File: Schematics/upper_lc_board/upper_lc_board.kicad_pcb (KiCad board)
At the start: 4 copper layers, 69.5 x 60 mm, 125 parts, among them J1 Stack Male Edge Connector, J3 PT1, J4 PT2, J5 SOL_CONN, J6 SOL2_CONN, J7 TC, Q1 MOSFET_BSS138, U1 ESP32-S3-WROOM-1-N16R2, U10 OA-TLV9001IDCK, U11 OA-TLV9001IDCK, U2 CAN_TRX_SN65HVD230DR, U3 PD_D3V3XA4B10LP, U4 PMUX_TPS2121RUXR, U5 TMP117MAIDRVR, U6 TLV75801PDRV, U7 ADC_ADS131M04IPWR, U8 SSR_VO1400AEFTR, U9 OA-TLV9001IDCK

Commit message: temp commit for layout work
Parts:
- removed BOOT, RESET: ~, Button_Switch_SMD:SW_Push_1P1T_XKB_TS-1187A
- removed the C18 at (140.6, 19.8)
- removed CAN: CAN_LED, LED_SMD:LED_0805_2012Metric
- removed FAULT: FAULT_LED, LED_SMD:LED_1206_3216Metric
- removed HALL S: HAL_SENS, 53048-0310:53048-0310
- removed the R18 at (140.6, 25.7)
- removed the R19 at (102.6, 29.5)
- removed SOL1, SOL2: SOL_LED, LED_SMD:LED_0805_2012Metric
- removed USB: USB_LED, LED_SMD:LED_0603_1608Metric
- removed WIFI: WIFI_LED, LED_SMD:LED_0805_2012Metric
- added C30: 0.1uF, Capacitor_SMD:C_0603_1608Metric, F.Cu at (111.0, 61.2)
- added C31: 0.1uF, Capacitor_SMD:C_0603_1608Metric, F.Cu at (111.0, 63.7)
- added D13: D_TVS, SMBJ28A:DIOM5436X244N, F.Cu at (123.0, 63.8)
- added D18: D_TVS, SMBJ28A:DIOM5436X244N, F.Cu at (123.0, 69.0)
- added D19: D_TVS, SMBJ28A:DIOM5436X244N, F.Cu at (123.0, 74.2)
- added R42: 4.7k, Resistor_SMD:R_0402_1005Metric, F.Cu at (114.5, 60.9)
- added R43: 4.7k, Resistor_SMD:R_0402_1005Metric, F.Cu at (114.5, 62.9)
- added R44: 10k, Resistor_SMD:R_0402_1005Metric, F.Cu at (114.5, 64.9)
- added R45: 10k, Resistor_SMD:R_0402_1005Metric, F.Cu at (114.5, 66.9)
- added R46: 1M, Resistor_SMD:R_0603_1608Metric, F.Cu at (111.0, 66.2)
- added R47: 1M, Resistor_SMD:R_0603_1608Metric, F.Cu at (111.0, 68.7)
- added U12: OA-TLV9001IDCK, Package_TO_SOT_SMD:SOT-353_SC-70-5, F.Cu at (122.5, 58.1)
- C10, C9: value 1uF_12V -> 1uF
- C12: value 0.1uF_12V -> 0.1uF
- C13: value 10uF_12V -> 10uF
- R1, R10, R13, R14, R15, R17 (x2), R18 (x2), R19 (x2), R2, R22, R23, R24, R25, R26, R28, R29, R3, R30, R31, R32, R33, R34, R35, R36, R37, R38, R39, R4, R40, R41, R5, R6, R7, R8, R9: footprint Capacitor_SMD:C_0402_1005Metric -> Resistor_SMD:R_0402_1005Metric
- R11: value 5k -> 68k; footprint Capacitor_SMD:C_0402_1005Metric -> Resistor_SMD:R_0402_1005Metric
- R12: value 5k -> 18k; footprint Capacitor_SMD:C_0402_1005Metric -> Resistor_SMD:R_0402_1005Metric
- R16 (x3): value 3.2k -> 1.2k; footprint Capacitor_SMD:C_0402_1005Metric -> Resistor_SMD:R_0402_1005Metric
- R27: value 330 -> 4.7k; footprint Capacitor_SMD:C_0402_1005Metric -> Resistor_SMD:R_0402_1005Metric
- moved R40 45.6 mm to (96.0, 45.5)
- moved R41 45.6 mm to (96.0, 47.5)
- moved C25 41.6 mm to (124.3, 30.2)
- moved C23 38.0 mm to (124.3, 35.5)
- moved C22 38.0 mm to (124.3, 33.0)
- moved C27 36.7 mm to (124.5, 24.5)
- moved C28 36.7 mm to (124.5, 27.0)
- moved R19 30.8 mm to (99.0, 27.5)
- moved C24 23.5 mm to (120.2, 27.5)
- moved C17 23.4 mm to (120.0, 35.0)
- moved C19 23.4 mm to (120.0, 37.5)
- moved C22 21.6 mm to (120.3, 30.0)
- moved C23 21.6 mm to (120.3, 32.5)
- moved R32 13.7 mm to (96.0, 30.0)
- moved R33 13.7 mm to (96.0, 32.0)
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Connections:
- C10 pad 1: /Power Circuitry/3V3_USB -> GND
- C10 pad 2: GND -> /Power Circuitry/3V3_USB
- C12 pad 2: +3V3 -> Net-(U4-SS)
- C9 pad 1: /Power Circuitry/3V3_BP -> GND
- C9 pad 2: GND -> /Power Circuitry/3V3_BP
- J7 pad 1: /Sensor Circuitry/TC_N -> /Sensor Circuitry/TC_P
- J7 pad 2: /Sensor Circuitry/TC_P -> /Sensor Circuitry/TC_N
- R11 pad 1: Net-(U4-~{CE}) -> Net-(U4-ILIM)
- R11 pad 2: /Power Circuitry/3V3_USB -> GND
- R12 pad 1: Net-(U5-~{CE}) -> /Power Circuitry/3V3_USB
- R12 pad 2: /Power Circuitry/3V3_BP -> Net-(U4-CP2)
- R16 pad 2: /Sensor Circuitry/HALL_OUT -> Net-(U9-+) (x3)
- R17 pad 1: /Sensor Circuitry/HALL_OUT -> Net-(U9-+) (x2)
- R18 pad 1: GND -> Net-(J3-Pin_2) (x2)
- R18 pad 2: Net-(U9-AIN0P) -> GND (x2)
- R19 pad 1: GND -> Net-(J4-Pin_2) (x2)
- R19 pad 2: Net-(U9-AIN1P) -> GND (x2)
- R25 pad 1: +3V3 -> Net-(U4-CP2)
- R25 pad 2: Net-(Y1-OE) -> GND
- R27 pad 1: GPIO_11 -> GPIO_38
- R27 pad 2: Net-(D13-K) -> +3V3

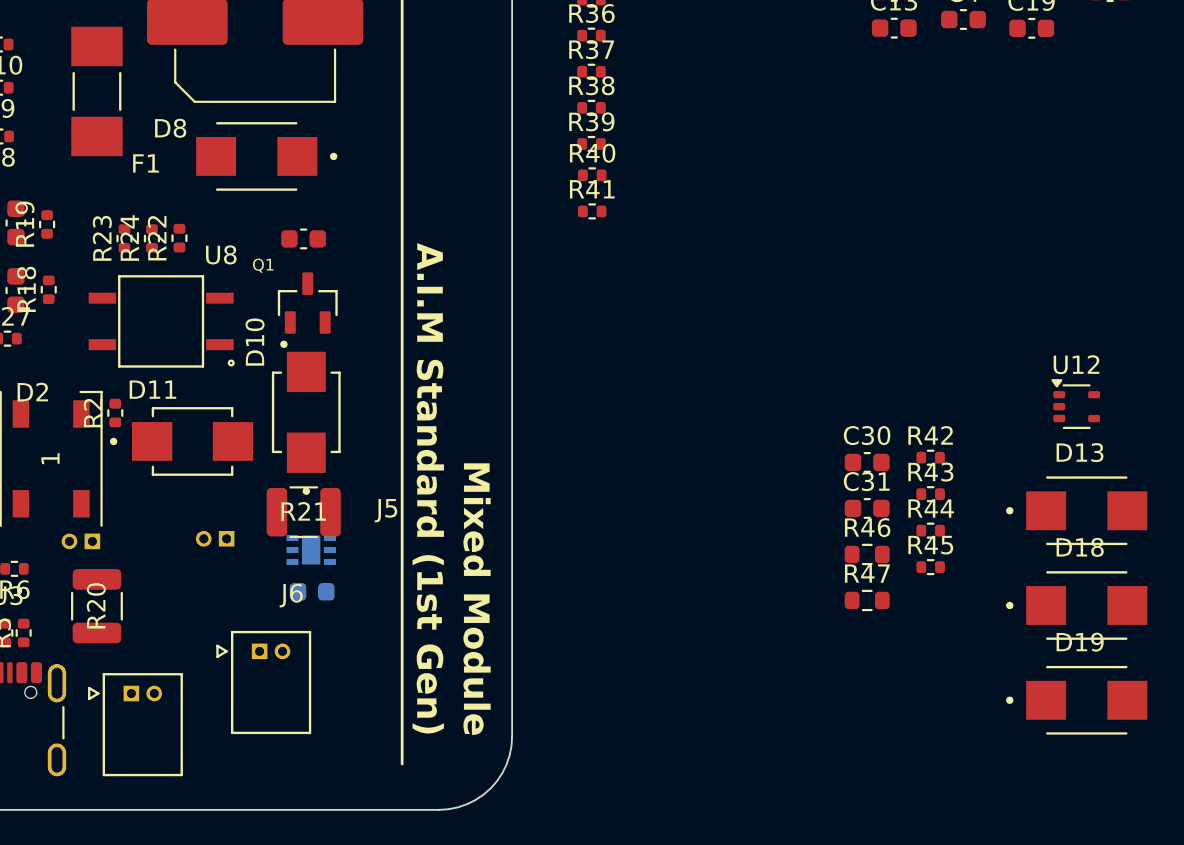
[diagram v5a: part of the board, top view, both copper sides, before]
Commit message: update schematic & board with smaller diode footprints
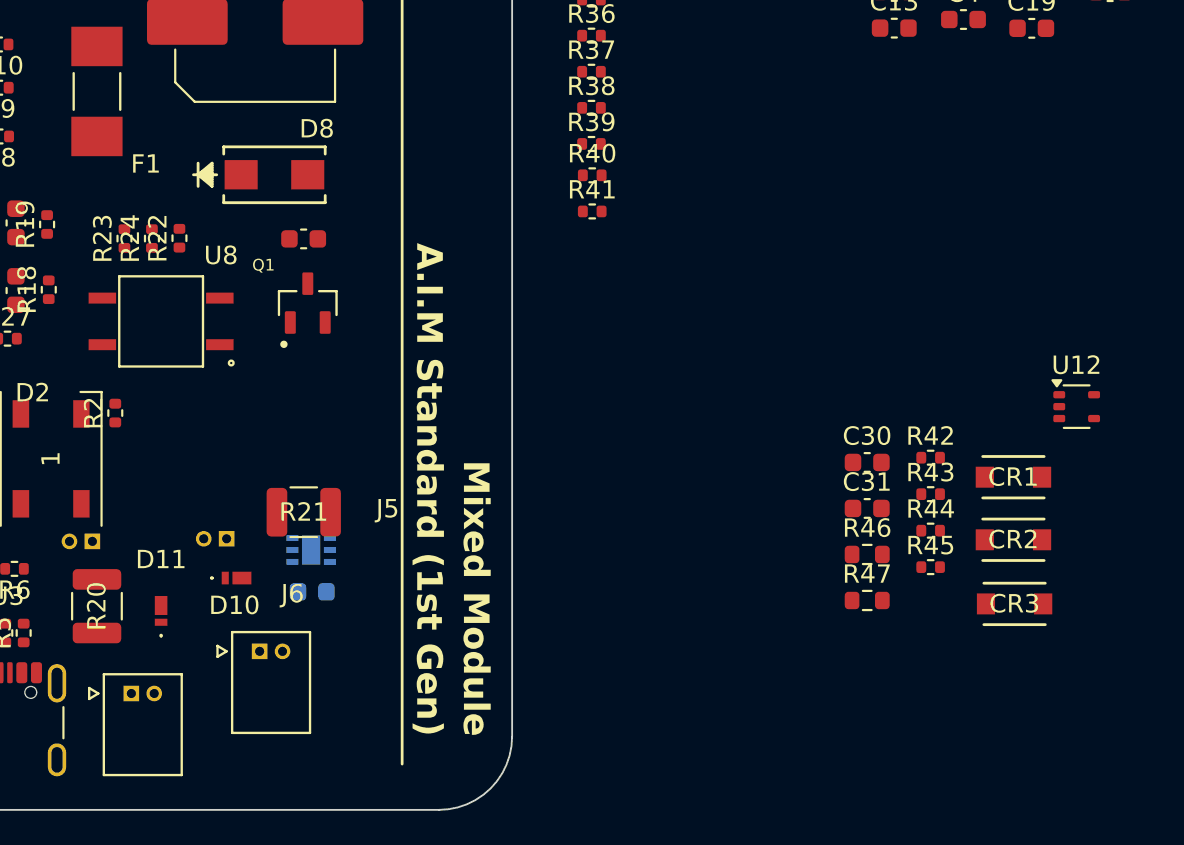
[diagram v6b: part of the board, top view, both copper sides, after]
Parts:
- removed D13, D18, D19: D_TVS, SMBJ28A:DIOM5436X244N
- added CR1: D_TVS_SMF5.0CA, SMF5_0CA:SOD-123F_LTF-L, F.Cu at (119.0, 62.0)
- added CR2: D_TVS_SMF5.0CA, SMF5_0CA:SOD-123F_LTF-L, F.Cu at (119.0, 65.4)
- added CR3: D_TVS_SMF5.0CA, SMF5_0CA:SOD-123F_LTF-L, F.Cu at (119.1, 68.9)
- D10, D11: footprint SK44BL-TP:DIOM4336X265N -> D_FB_SDM4A:SDM4A40EP37B
- D8: footprint SMBJ28A:DIOM5436X244N -> SMA6L30A:SMASeries_LTF-L
- moved D10 9.81 mm to (76.6, 67.5), turned to 0 degrees
- moved D11 9.40 mm to (72.5, 69.3), turned to 90 degrees
- moved D8 1.39 mm to (78.7, 45.5), turned to 0 degrees

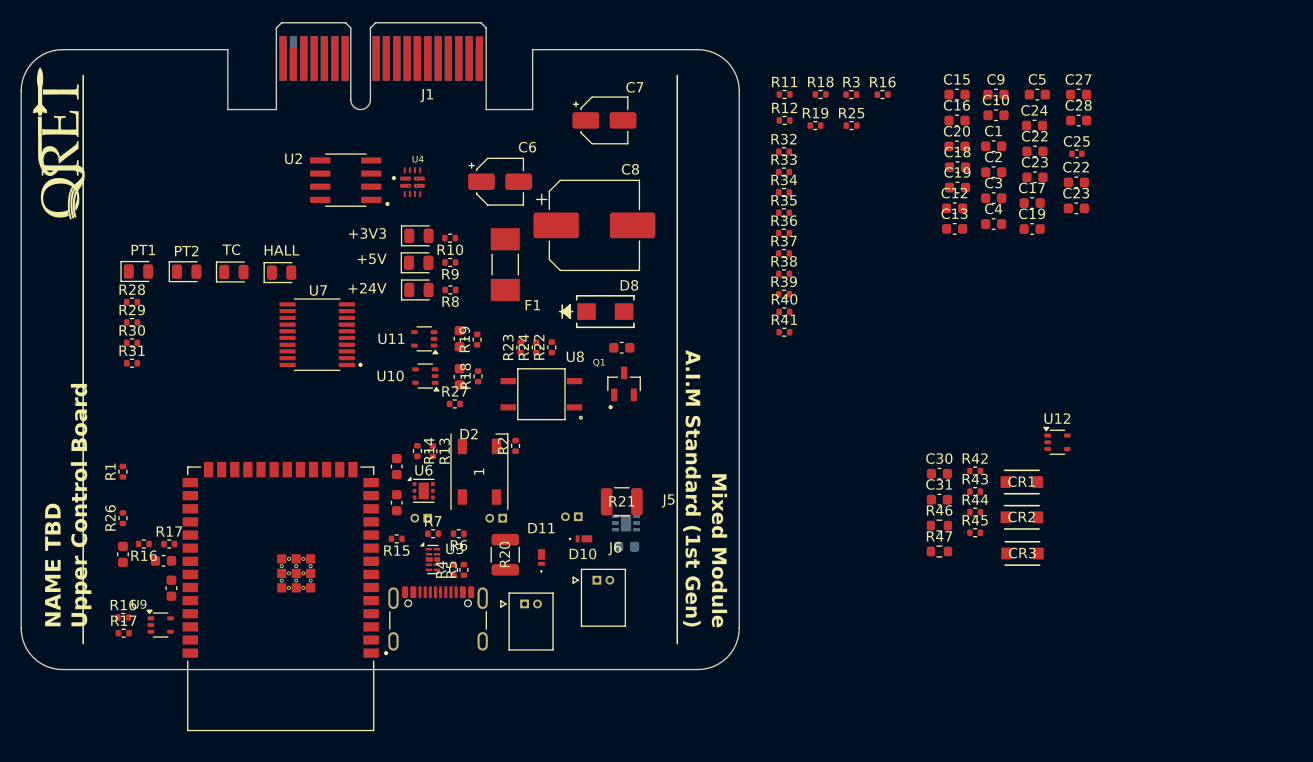
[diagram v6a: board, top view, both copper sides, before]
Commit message: fix footprint designators
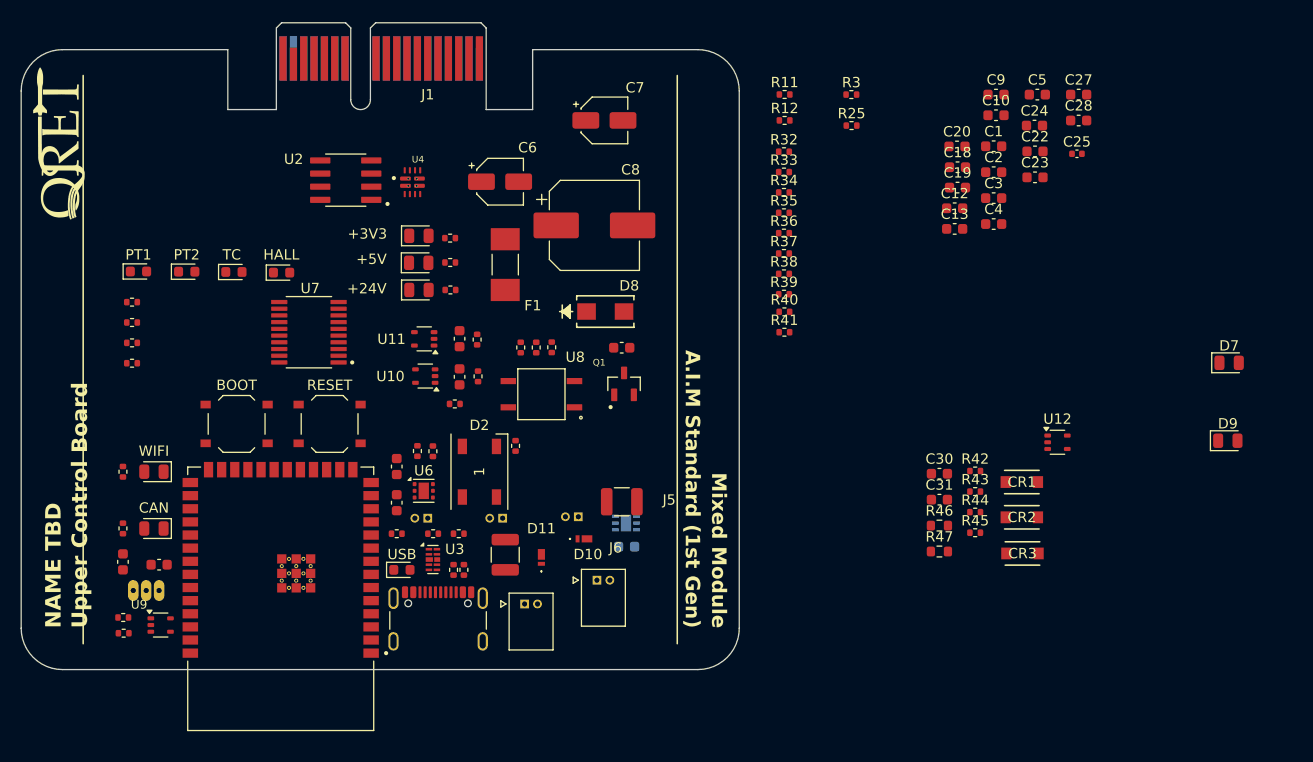
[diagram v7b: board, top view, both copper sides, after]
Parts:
- removed the C15 at (112.7, 24.5)
- removed the C15 at (36.7, 72.3)
- removed the C16 at (112.7, 27.0)
- removed the C17 at (120.0, 35.0)
- removed the C19 at (120.0, 37.5)
- removed the C22 at (124.3, 33.0)
- removed the C23 at (124.3, 35.5)
- removed the R16 at (34.0, 68.0)
- removed the R16 at (105.5, 24.5)
- removed the R17 at (36.5, 68.0)
- removed the R18 at (99.5, 24.5)
- removed the R19 at (99.0, 27.5)
- added BOOT: ~, Button_Switch_SMD:SW_Push_1P1T_XKB_TS-1187A, F.Cu at (43.0, 56.4)
- added CAN: CAN_LED, LED_SMD:LED_0805_2012Metric, F.Cu at (35.0, 66.5)
- added D7: SOL_LED, LED_SMD:LED_0805_2012Metric, F.Cu at (139.1, 50.5)
- added D9: SOL_LED, LED_SMD:LED_0805_2012Metric, F.Cu at (138.9, 58.0)
- added J2: HAL_SENS, 53048-0310:53048-0310, B.Cu at (34.2, 72.5)
- added RESET: ~, Button_Switch_SMD:SW_Push_1P1T_XKB_TS-1187A, F.Cu at (52.0, 56.4)
- added USB: USB_LED, LED_SMD:LED_0603_1608Metric, F.Cu at (59.0, 70.5)
- added WIFI: WIFI_LED, LED_SMD:LED_0805_2012Metric, F.Cu at (35.0, 61.0)
- D14, D15, D16, D17: footprint LED_SMD:LED_0805_2012Metric -> LED_SMD:LED_0603_1608Metric
- moved R26 0.99 mm to (32.0, 66.5)
- moved U7 0.83 mm to (50.0, 47.5)
- moved C15 0.72 mm to (32.0, 69.7)
- moved C16 0.56 mm to (35.5, 70.0)
- moved R15 0.50 mm to (58.5, 67.0)

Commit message: ..
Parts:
- removed the CAN at (35.0, 66.5)
- removed the WIFI at (35.0, 61.0)
- added CAN: CAN_LED, LED_SMD:LED_1206_3216Metric, F.Cu at (35.1, 66.9)
- added WIFI: WIFI_LED, LED_SMD:LED_1206_3216Metric, F.Cu at (35.0, 61.0)
- BOOT: value ~ -> BOOT
- D14, D15, D16, D17: footprint LED_SMD:LED_0603_1608Metric -> LED_SMD:LED_0805_2012Metric
- D7: value SOL_LED -> SOL1_LED
- D9: value SOL_LED -> SOL2_LED
- RESET: value ~ -> Reset
- moved R18 23.8 mm to (42.8, 49.0)
- moved C17 23.8 mm to (41.0, 49.0)
- moved C26 23.8 mm to (41.0, 45.3)
- moved R19 23.8 mm to (42.7, 45.4)
- moved U10 23.8 mm to (37.6, 49.0)
- moved U11 23.8 mm to (37.5, 45.4)
- moved U7 13.8 mm to (63.6, 49.8)
- moved R8 8.79 mm to (56.9, 37.9), turned to 0 degrees
- moved R10 8.12 mm to (56.9, 42.9), turned to 0 degrees
- moved R9 6.79 mm to (56.9, 40.5), turned to 0 degrees
- moved D5 5.59 mm to (59.9, 37.9), turned to 180 degrees
- moved D3 4.99 mm to (59.9, 43.1), turned to 180 degrees
- moved D15 3.68 mm to (38.4, 38.0)
- moved D16 3.68 mm to (43.0, 38.0)
- moved R28 3.68 mm to (33.1, 40.9)
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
